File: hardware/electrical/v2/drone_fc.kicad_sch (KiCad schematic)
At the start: 29 parts, among them J1 Cortex_SWD_10P, J2 ESC_4IN1_JST_SH, U1 TLV75533PDBVR, U2 LMR50410_Buck, U3 MDBT53-P1M, U4 ICM-42688-P

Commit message: swd: switch J1 to Tag-Connect TC2050-IDC-NL cableless footprint
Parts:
- J1: footprint Connector_PinHeader_1.27mm:PinHeader_2x05_P1.27mm_Vertical_SMD -> Connector:Tag-Connect_TC2050-IDC-NL_2x05_P1.27mm_Vertical
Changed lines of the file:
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@@
 			)
 		)
-		(property "Footprint" "Connector_PinHeader_1.27mm:PinHeader_2x05_P1.27mm_Vertical_SMD"
+		(property "Footprint" "Connector:Tag-Connect_TC2050-IDC-NL_2x05_P1.27mm_Vertical"
 			(at 76.2 175.26 0)
 			(hide yes)

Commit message: imu: fix ICM-42688-P symbol pin numbers to match real package pinout
Same bug class as the MDBT53 fix: the ICM_42688_P symbol's pins were
numbered by schematic drawing order (1..14), not the real InvenSense
LGA-14 pad numbers used by the footprint. Verified against the pinout
table in doc/hardware/ds-000347-icm-42688-p-v1.6.pdf and remapped every
pin to its real pad number.

Two pins were actively dangerous, not just mislabeled:
- Real pin 8 (VDD) was marked NC - the IMU's core supply pin was
  unconnected.
- Real pin 11 (RESV, datasheet permits only NC or GND) had +3V3 wired
  to it via the symbol's old pin 7 ("RESV_VDD").

Fixed by renumbering so the pin that was already correctly wired to
+3V3 (old pin 13, "VDD") becomes the real VDD pin (8) - no wire changes
needed there. The one pin that could not be fixed by renumbering alone
(real pin 11, previously on +3V3) had its wire removed and is now
explicitly marked no-connect, a datasheet-legal state for that pin.

Verified via netlist re-export at each step rather than by inspection
alone, after an initial manual wire-trace turned out to be wrong.

ERC: 0 errors, 1 pre-existing cosmetic warning (a dangling wire stub
left for manual cleanup in the KiCad GUI rather than a second blind
text edit).
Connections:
- net +3V3: now also U4.5 (VDDIO), U4.8 (VDD); no longer U4.13 (VDD), U4.3 (VDDIO), U4.7 (RESV_VDD)
- net GND: now also U4.2 (RESV_2), U4.3 (RESV_3), U4.7 (RESV_GND); no longer U4.12 (GND), U4.4 (GND), U4.5 (GND)
- net IMU_CS: now also U4.12 (AP_CS); no longer U4.9 (AP_CS)
- net IMU_INT1: now also U4.4 (INT1); no longer U4.2 (INT1)
- net SPI_MOSI: now also U4.14 (AP_SDI); no longer U4.11 (AP_SDI)
- net SPI_SCK: now also U4.13 (AP_SCLK); no longer U4.10 (AP_SCLK)
- no-connect marks 7 -> 8
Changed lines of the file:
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@@
+	)
+	(no_connect
+		(at 350.52 124.46)
 	)
 	(no_connect
@@
 	)
 	(wire
-		(pts
-			(xy 350.52 124.46) (xy 360.68 124.46)
-		)
-		(stroke
-			(width 0)
-			(type default)
-		)
-	)
-	(wire

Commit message: bom: add MPN field for C1, C5, L1 with verified real parts
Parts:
- C1: footprint Capacitor_SMD:C_1210_3225Metric -> Capacitor_SMD:C_1206_3216Metric; MPN (none) -> CL31B106KBHNNNE
- C5: MPN (none) -> GRM21BR61A226ME44
- J1: footprint Connector:Tag-Connect_TC2050-IDC-NL_2x05_P1.27mm_Vertical -> Connector_PinHeader_1.27mm:PinHeader_2x05_P1.27mm_Vertical_SMD
- L1: MPN (none) -> MLZ2012M150WT000
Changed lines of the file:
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@@
-	)
-	(junction
-		(at 360.68 119.38)
-		(diameter 0.9144)
-		(color 0 0 0 0)
 	)
 	(junction
@@
 	)
 	(no_connect
+		(at 350.52 124.46)
+	)
+	(no_connect
 		(at 193.04 160.02)
 	)
@@
 	)
 	(no_connect
-		(at 350.52 124.46)
-	)
-	(no_connect
 		(at 193.04 129.54)
 	)
@@
 		(pts
 			(xy 350.52 119.38) (xy 360.68 119.38)
-		)
-		(stroke
-			(width 0)
-			(type default)
-		)
-	)
-	(wire
-		(pts
-			(xy 360.68 119.38) (xy 360.68 124.46)
 		)
 		(stroke
@@
 			)
 		)
+		(property "MPN" "GRM21BR61A226ME44"
+			(at 140.97 91.44 0)
+			(hide yes)
+			(show_name no)
+			(do_not_autoplace no)
+			(effects
+				(font
+					(size 1.27 1.27)
+				)
+			)
+		)
 		(property "Datasheet" "~"
 			(at 140.97 91.44 0)
@@
 			)
 		)
-		(property "Footprint" "Connector:Tag-Connect_TC2050-IDC-NL_2x05_P1.27mm_Vertical"
+		(property "Footprint" "Connector_PinHeader_1.27mm:PinHeader_2x05_P1.27mm_Vertical_SMD"
 			(at 76.2 175.26 0)
 			(hide yes)
@@
 	)
 	(symbol
-		(lib_name "Capacitor_1")
 		(lib_id "drone_fc_v2_symbols:Capacitor")
 		(at 41.91 120.65 0)
@@
 			)
 		)
+		(property "MPN" "MLZ2012M150WT000"
+			(at 111.76 83.82 0)
+			(hide yes)
+			(show_name no)
+			(do_not_autoplace no)
+			(effects
+				(font
+					(size 1.27 1.27)
+				)
+			)
+		)
 		(property "Datasheet" "~"
 			(at 111.76 83.82 0)
@@
 			)
 		)
-		(property "Footprint" "Capacitor_SMD:C_1210_3225Metric"
+		(property "Footprint" "Capacitor_SMD:C_1206_3216Metric"
 			(at 41.91 88.9 0)
 			(hide yes)
+			(show_name no)
+			(do_not_autoplace no)
+			(effects
+				(font
+					(size 1.27 1.27)
+				)
+			)
+		)
+		(property "MPN" "CL31B106KBHNNNE"
+			(at 41.91 88.9 0)
+			(hide yes)

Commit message: bom: add verified MPN for all resistors, LEDs, TVS diode, and U2
Populates the remaining MPN gaps, each confirmed against a live
distributor listing rather than guessed from memory (several earlier
memory-based guesses this session turned out not to exist):

- R1 (66.5K), R2 (22.1K), R3/R4 (1K), R5-R9 (10K): Yageo RC0402FR-07
  1% E96 series - RC0402FR-0766K5L, RC0402FR-0722K1L, RC0402FR-071KL,
  RC0402FR-0710KL.
- D1 (Green_Status): Lite-On LTST-C281KGKT.
- D2 (Blue_Radio): Lite-On LTST-C281TBKT.
- TVS1: Littelfuse SMAJ24A (the value was already the generic
  industry part number; this pins one specific vendor's orderable
  code for the BOM).
- U2 (LMR50410): TI's actual orderable code LMR50410XDBVR - the
  Value field only ever held the descriptive "LMR50410_Buck", not an
  orderable part number.

Every reference in the design now has a real, sourceable part behind
it. ERC: 0 errors, 0 warnings.
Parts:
- D1: MPN (none) -> LTST-C281KGKT
- D2: MPN (none) -> LTST-C281TBKT
- R1: MPN (none) -> RC0402FR-0766K5L
- R2: MPN (none) -> RC0402FR-0722K1L
- R3, R4: MPN (none) -> RC0402FR-071KL
- R5, R6, R7, R8, R9: MPN (none) -> RC0402FR-0710KL
- TVS1: MPN (none) -> SMAJ24A
- U2: MPN (none) -> LMR50410XDBVR
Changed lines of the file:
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@@
 			)
 		)
+		(property "MPN" "LTST-C281KGKT"
+			(at 210.82 208.28 0)
+			(hide yes)
+			(show_name no)
+			(do_not_autoplace no)
+			(effects
+				(font
+					(size 1.27 1.27)
+				)
+			)
+		)
 		(property "Datasheet" "~"
 			(at 210.82 208.28 0)
@@
 			)
 		)
+		(property "MPN" "RC0402FR-0710KL"
+			(at 274.32 218.44 0)
+			(hide yes)
+			(show_name no)
+			(do_not_autoplace no)
+			(effects
+				(font
+					(size 1.27 1.27)
+				)
+			)
+		)
 		(property "Datasheet" "~"
 			(at 274.32 218.44 0)
@@
 			)
 		)
+		(property "MPN" "RC0402FR-0710KL"
+			(at 293.37 218.44 0)
+			(hide yes)
+			(show_name no)
+			(do_not_autoplace no)
+			(effects
+				(font
+					(size 1.27 1.27)
+				)
+			)
+		)
 		(property "Datasheet" "~"
 			(at 293.37 218.44 0)
@@
 			)
 		)
+		(property "MPN" "RC0402FR-071KL"
+			(at 210.82 226.06 0)
+			(hide yes)
+			(show_name no)
+			(do_not_autoplace no)
+			(effects
+				(font
+					(size 1.27 1.27)
+				)
+			)
+		)
 		(property "Datasheet" "~"
 			(at 210.82 226.06 0)
@@
 			)
 		)
+		(property "MPN" "LTST-C281TBKT"
+			(at 220.98 208.28 0)
+			(hide yes)
+			(show_name no)
+			(do_not_autoplace no)
+			(effects
+				(font
+					(size 1.27 1.27)
+				)
+			)
+		)
 		(property "Datasheet" "~"
 			(at 220.98 208.28 0)
@@
 			)
 		)
+		(property "MPN" "RC0402FR-071KL"
+			(at 220.98 226.06 0)
+			(hide yes)
+			(show_name no)
+			(do_not_autoplace no)
+			(effects
+				(font
+					(size 1.27 1.27)
+				)
+			)
+		)
 		(property "Datasheet" "~"
 			(at 220.98 226.06 0)
@@
 			)
 		)
+		(property "MPN" "SMAJ24A"
+			(at 31.75 88.9 0)
+			(hide yes)
+			(show_name no)
+			(do_not_autoplace no)
+			(effects
+				(font
+					(size 1.27 1.27)
+				)
+			)
+		)
 		(property "Datasheet" "~"
 			(at 31.75 88.9 0)
@@
 			)
 		)
+		(property "MPN" "RC0402FR-0710KL"
+			(at 302.26 218.44 0)
+			(hide yes)
+			(show_name no)
+			(do_not_autoplace no)
+			(effects
+				(font
+					(size 1.27 1.27)
+				)
+			)
+		)
 		(property "Datasheet" "~"
 			(at 302.26 218.44 0)
@@
 			)
 		)
+		(property "MPN" "RC0402FR-0710KL"
+			(at 295.91 100.33 0)
+			(hide yes)
+			(show_name no)
+			(do_not_autoplace no)
+			(effects
+				(font
+					(size 1.27 1.27)
+				)
+			)
+		)
 		(property "Datasheet" "~"
 			(at 295.91 100.33 0)
@@
 			)
 		)
+		(property "MPN" "RC0402FR-0722K1L"
+			(at 124.46 105.41 0)
+			(hide yes)
+			(show_name no)
+			(do_not_autoplace no)
+			(effects
+				(font
+					(size 1.27 1.27)
+				)
+			)
+		)
 		(property "Datasheet" "~"
 			(at 124.46 105.41 0)
@@
 			)
 		)
+		(property "MPN" "RC0402FR-0766K5L"
+			(at 124.46 91.44 0)
+			(hide yes)
+			(show_name no)
+			(do_not_autoplace no)
+			(effects
+				(font
+					(size 1.27 1.27)
+				)
+			)
+		)
 		(property "Datasheet" "~"
 			(at 124.46 91.44 0)
@@
 			)
 		)
+		(property "MPN" "LMR50410XDBVR"
+			(at 72.39 88.9 0)
+			(hide yes)
+			(show_name no)
+			(do_not_autoplace no)
+			(effects
+				(font
+					(size 1.27 1.27)
+				)
+			)
+		)
 		(property "Datasheet" "https://www.ti.com/lit/ds/symlink/lmr50410.pdf"
 			(at 72.39 88.9 0)
@@
 			(at 283.21 218.44 0)
 			(hide yes)
+			(show_name no)
+			(do_not_autoplace no)
+			(effects
+				(font
+					(size 1.27 1.27)
+				)
+			)
+		)
+		(property "MPN" "RC0402FR-0710KL"
+			(at 283.21 218.44 0)
+			(hide yes)

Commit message: swd: fix J1 footprint regression, generate BOM
Generating the first real BOM (hardware/electrical/v2/drone_fc-bom.csv)
surfaced a regression: J1's footprint had silently reverted from
Tag-Connect back to the generic pin header. Same root cause as the
earlier passive-footprint resets - a per-instance override that
diverged from its symbol's library default gets discarded by the next
Update Symbols from Library resync, regardless of component type.

Unlike the passives, Cortex_SWD_10P is not a shared generic symbol -
it has exactly one instance (J1) in the whole design, the same as
MDBT53_P1M/TLV75533PDBVR/LMR50410_Buck. So here the correct fix is to
set the library's own default Footprint to Tag-Connect, matching how
those single-purpose symbols already store their real footprint.
Library and instance now agree; there is nothing left for a resync to
revert.

ERC: 0 errors, 0 warnings.
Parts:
- J1: footprint Connector_PinHeader_1.27mm:PinHeader_2x05_P1.27mm_Vertical_SMD -> Connector:Tag-Connect_TC2050-IDC-NL_2x05_P1.27mm_Vertical
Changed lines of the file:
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@@
 			)
 		)
-		(property "Footprint" "Connector_PinHeader_1.27mm:PinHeader_2x05_P1.27mm_Vertical_SMD"
+		(property "Footprint" "Connector:Tag-Connect_TC2050-IDC-NL_2x05_P1.27mm_Vertical"
 			(at 76.2 175.26 0)
 			(hide yes)

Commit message: bom: add remaining MPN for decoupling caps, ESC connector, and ICs
Fills in the last MPN gaps left after d08bbe8/773a07c: 1uF/100nF/10nF/4.7uF decoupling caps (Murata/KEMET), the ESC 4-in-1 JST-SH connector (SM08B-SRSS-TB), and U1/U3/U4 (whose MPN is identical to their existing Value string). J1's Tag-Connect footprint is left without an MPN deliberately - it's a pogo-pad pattern, not a populated part. BOM regenerated via kicad-cli sch export bom; ERC still 0 violations.
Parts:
- C10: MPN (none) -> C0402C103K5RECAUTO
- C2, C3: MPN (none) -> GRM155R61C105KA12D
- C4, C7, C8, C9: MPN (none) -> GRM155R71H104KE14D
- C6: MPN (none) -> GRM188R61A475KAAJD
- J2: MPN (none) -> SM08B-SRSS-TB
- U1: MPN (none) -> TLV75533PDBVR
- U3: MPN (none) -> MDBT53-P1M
- U4: MPN (none) -> ICM-42688-P
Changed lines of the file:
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@@
 			)
 		)
+		(property "MPN" "GRM155R61C105KA12D"
+			(at 41.91 120.65 0)
+			(hide yes)
+			(show_name no)
+			(do_not_autoplace no)
+			(effects
+				(font
+					(size 1.27 1.27)
+				)
+			)
+		)
 		(property "Datasheet" "~"
 			(at 41.91 120.65 0)
@@
 			)
 		)
+		(property "MPN" "GRM155R61C105KA12D"
+			(at 88.9 120.65 0)
+			(hide yes)
+			(show_name no)
+			(do_not_autoplace no)
+			(effects
+				(font
+					(size 1.27 1.27)
+				)
+			)
+		)
 		(property "Datasheet" "~"
 			(at 88.9 120.65 0)
@@
 			)
 		)
+		(property "MPN" "GRM155R71H104KE14D"
+			(at 95.25 88.9 0)
+			(hide yes)
+			(show_name no)
+			(do_not_autoplace no)
+			(effects
+				(font
+					(size 1.27 1.27)
+				)
+			)
+		)
 		(property "Datasheet" "~"
 			(at 95.25 88.9 0)
@@
 			)
 		)
+		(property "MPN" "GRM155R71H104KE14D"
+			(at 199.39 85.09 0)
+			(hide yes)
+			(show_name no)
+			(do_not_autoplace no)
+			(effects
+				(font
+					(size 1.27 1.27)
+				)
+			)
+		)
 		(property "Datasheet" "~"
 			(at 199.39 85.09 0)
@@
 			)
 		)
+		(property "MPN" "C0402C103K5RECAUTO"
+			(at 386.08 119.38 0)
+			(hide yes)
+			(show_name no)
+			(do_not_autoplace no)
+			(effects
+				(font
+					(size 1.27 1.27)
+				)
+			)
+		)
 		(property "Datasheet" "~"
 			(at 386.08 119.38 0)
@@
 			)
 		)
+		(property "MPN" "ICM-42688-P"
+			(at 330.2 124.46 0)
+			(hide yes)
+			(show_name no)
+			(do_not_autoplace no)
+			(effects
+				(font
+					(size 1.27 1.27)
+				)
+			)
+		)
 		(property "Datasheet" "https://invensense.tdk.com/download-pdf/icm-42688-p-datasheet/"
 			(at 330.2 124.46 0)
@@
 			)
 		)
+		(property "MPN" "TLV75533PDBVR"
+			(at 69.85 120.65 0)
+			(hide yes)
+			(show_name no)
+			(do_not_autoplace no)
+			(effects
+				(font
+					(size 1.27 1.27)
+				)
+			)
+		)
 		(property "Datasheet" "https://www.ti.com/lit/ds/symlink/tlv755p.pdf"
 			(at 69.85 120.65 0)
@@
 			)
 		)
+		(property "MPN" "MDBT53-P1M"
+			(at 215.9 139.7 0)
+			(hide yes)
+			(show_name no)
+			(do_not_autoplace no)
+			(effects
+				(font
+					(size 1.27 1.27)
+				)
+			)
+		)
 		(property "Datasheet" "https://www.raytac.com/download/index.php?index_id=43"
 			(at 215.9 139.7 0)
@@
 			)
 		)
+		(property "MPN" "GRM155R71H104KE14D"
+			(at 373.38 119.38 0)
+			(hide yes)
+			(show_name no)
+			(do_not_autoplace no)
+			(effects
+				(font
+					(size 1.27 1.27)
+				)
+			)
+		)
 		(property "Datasheet" "~"
 			(at 373.38 119.38 0)
@@
 			)
 		)
+		(property "MPN" "GRM188R61A475KAAJD"
+			(at 177.8 85.09 0)
+			(hide yes)
+			(show_name no)
+			(do_not_autoplace no)
+			(effects
+				(font
+					(size 1.27 1.27)
+				)
+			)
+		)
 		(property "Datasheet" "~"
 			(at 177.8 85.09 0)
@@
 			)
 		)
+		(property "MPN" "SM08B-SRSS-TB"
+			(at 342.9 195.58 0)
+			(hide yes)
+			(show_name no)
+			(do_not_autoplace no)
+			(effects
+				(font
+					(size 1.27 1.27)
+				)
+			)
+		)
 		(property "Datasheet" "https://www.jst-mfg.com/product/pdf/eng/eSH.pdf"
 			(at 342.9 195.58 0)
@@
 			(at 189.23 85.09 0)
 			(hide yes)
+			(show_name no)
+			(do_not_autoplace no)
+			(effects
+				(font
+					(size 1.27 1.27)
+				)
+			)
+		)
+		(property "MPN" "GRM155R71H104KE14D"
+			(at 189.23 85.09 0)
+			(hide yes)

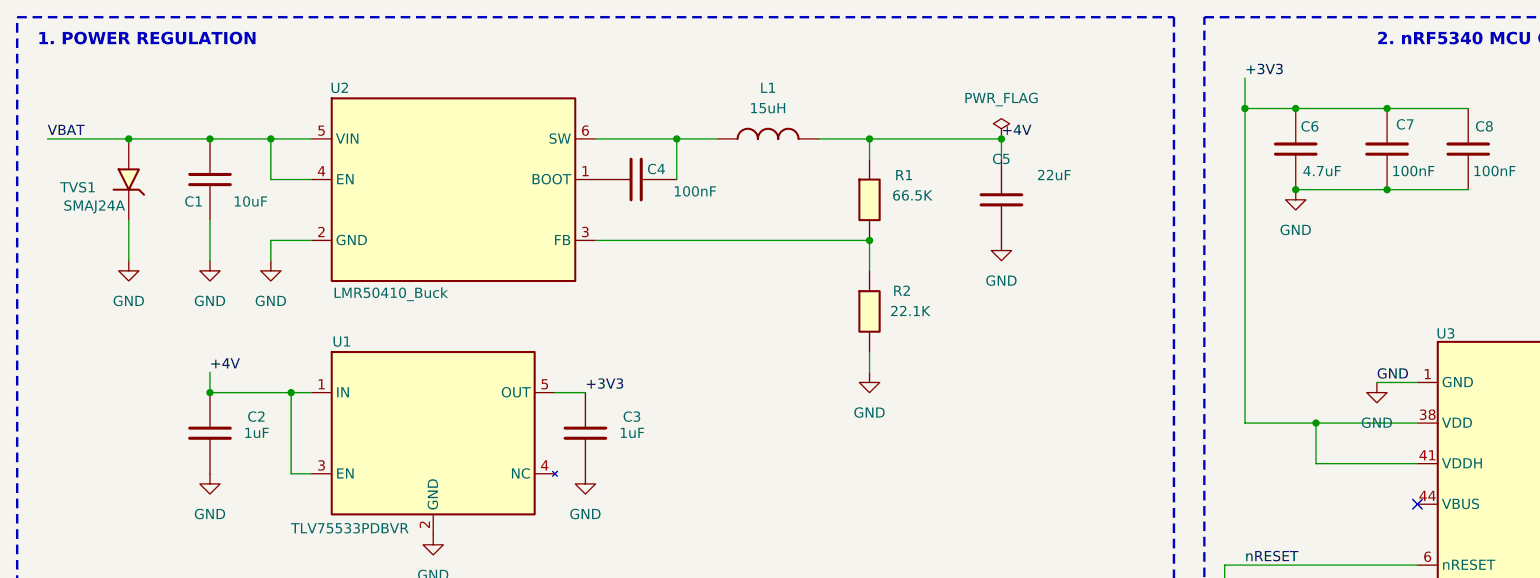
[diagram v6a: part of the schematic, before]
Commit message: layout: establish stack-compatible FC placement
Define the 20 mm ESC mounting pattern and board outline, place the flight-controller components around the stack, and preserve the MDBT53 antenna keepout at the board edge. Add labelled GND, VBAT, +4V, and +3V3 schematic test points with matching board pads. Repair the MDBT53 courtyard and route the first buck switch-node and +4V segments.\n\nERC is clean. PCB DRC has no electrical or mechanical errors; remaining findings are silkscreen-only while routing is in progress.
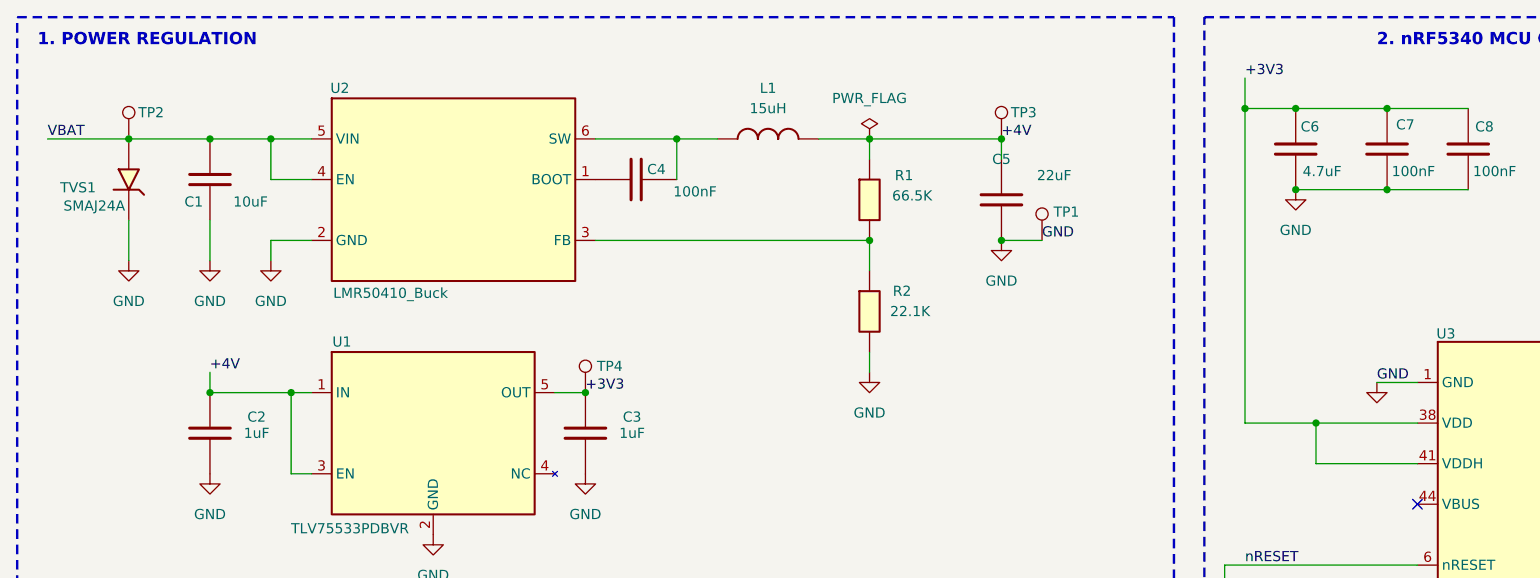
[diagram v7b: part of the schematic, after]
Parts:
- added TP1: GND, TestPoint:TestPoint_Pad_D1.0mm, symbol Connector:TestPoint
- added TP2: VBAT, TestPoint:TestPoint_Pad_D1.0mm, symbol Connector:TestPoint
- added TP3: +4V, TestPoint:TestPoint_Pad_D1.0mm, symbol Connector:TestPoint
- added TP4: +3V3, TestPoint:TestPoint_Pad_D1.0mm, symbol Connector:TestPoint
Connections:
- net +3V3: now also TP4.1
- net +4V: now also TP3.1
- net GND: now also TP1.1
- net VBAT: now also TP2.1

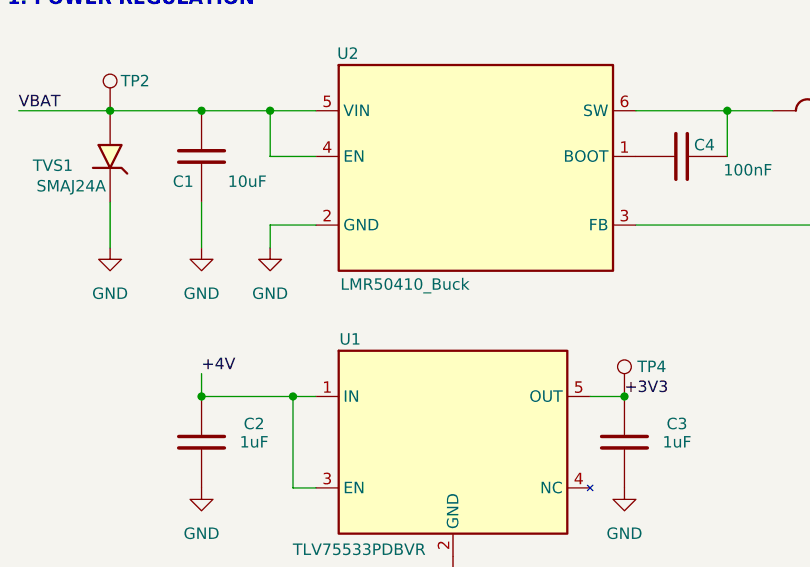
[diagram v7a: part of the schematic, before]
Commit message: layout: complete routing of the flight controller PCB
Every net on the nRF5340 carrier is now routed: 0 unconnected items, down
from 30 at the end of the previous session. No copper, clearance, short,
drill or dangling-item violations remain. The 23 outstanding DRC findings
are all silkscreen warnings - reference text over pads, label collisions
and text clipped by the board edge - which have no electrical or assembly
consequence on a 30 mm board populated with 0402s.

Also removes an accidental mirror on U2 that a crash-recovery autosave had
introduced. Mirroring a symbol relocates its pin endpoints while the wires
stay put, so every pin had swapped with its opposite across the centreline
(VIN with SW, GND with FB, BOOT with EN) - a real netlist fault rather than
a cosmetic flip. Adds the LMR50410 datasheet alongside the existing TLV755P.
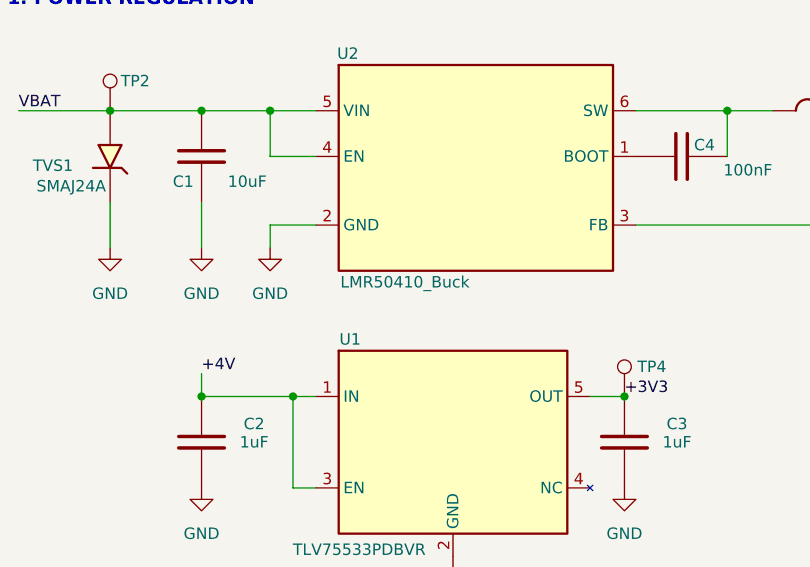
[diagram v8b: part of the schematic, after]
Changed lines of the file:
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@@
 		)
 		(property "Value" "LMR50410_Buck"
-			(at 64.516 103.124 0)
+			(at 64.516 102.87 0)
 			(show_name no)
 			(do_not_autoplace no)
